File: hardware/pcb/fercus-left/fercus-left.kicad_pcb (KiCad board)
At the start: 2 copper layers, 133 x 133 mm, 274 parts, among them J1 USB_C_Receptacle_USB2.0, J2 USB_C_Receptacle_USB2.0, J3 Conn_01x06_MountingPin, J5 Conn_01x03, Q1 BSS138, Q10 BSS138, Q2 BSS138, Q3 BSS138, Q4 BSS138, Q5 BSS138, Q6 BSS138, Q7 BSS138, Q8 BSS138, Q9 BSS138, SW1 SW_Push, SW2 SW_Push, SW3 SW_Push, SW4 SW_Push, SW6 SW_Push, SW7 SW_SPDT, SW8 SW_Push, U1 XC6206P332MR, U2 CH32V208CBU6, U3 ETA9084E10, Y1 32MHz, Y2 32.768kHz

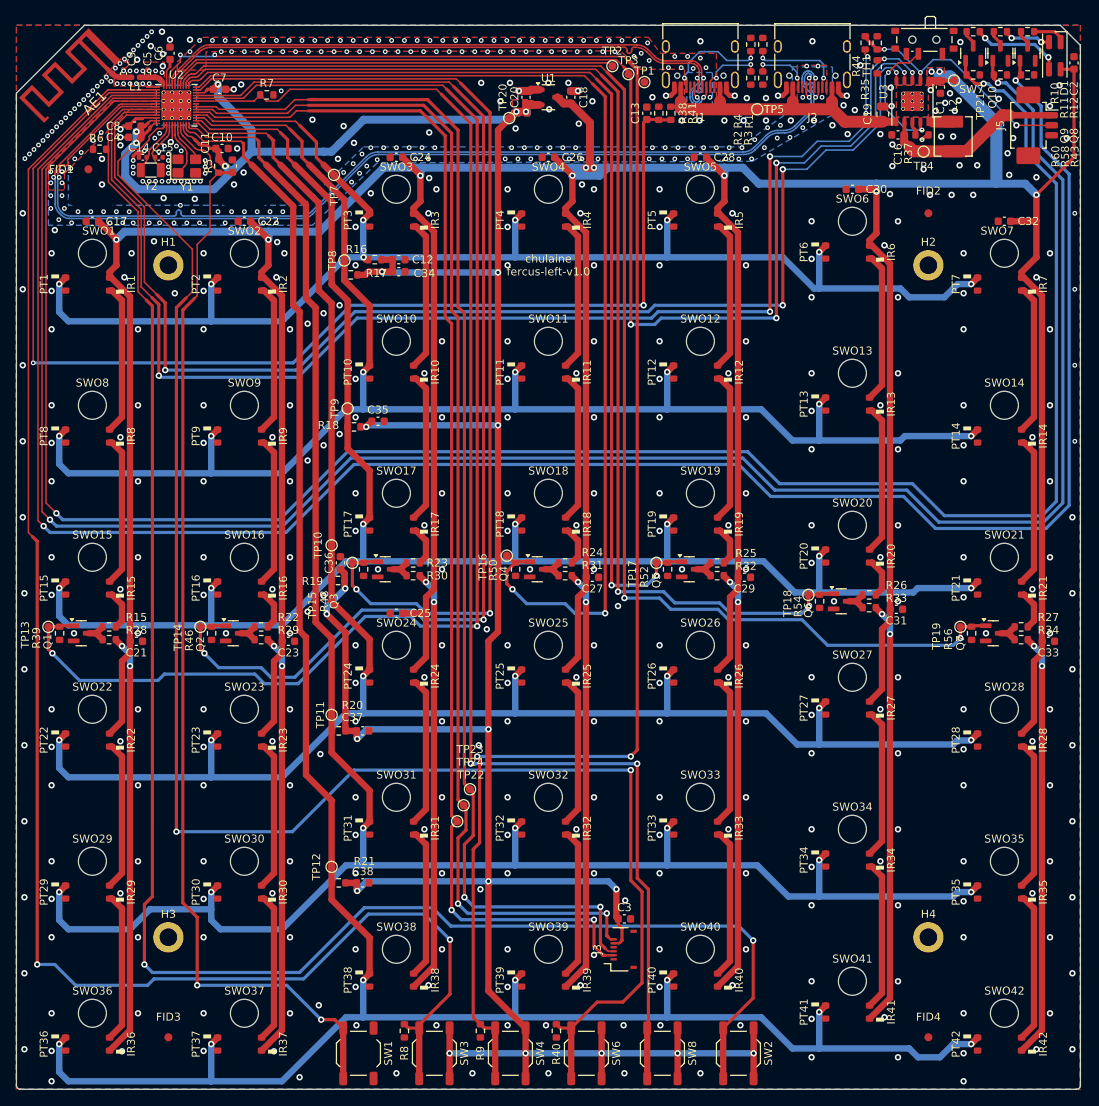
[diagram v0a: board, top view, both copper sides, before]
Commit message: merge
    fw:
    - fix usb product string, vid
    - add rf_phy_hop
    - add RF_BondingErase()
    - change default layout key fn to pause
    - fix power manager poweroff when usb disconnect
    - add usb compatibility interface

    hw:
    - change eta9084 iset resistor footprint to 0402
    - change fpc connector part
    - fix ir resistor value
    - change pcb thinkness to 1.6mm
    - fix footprint of pt and ir
    - fix rf ant trace
    - fix usb trace
    - add fercus-dongle-usb-c

    doc:
    - fix layout
    - add manual
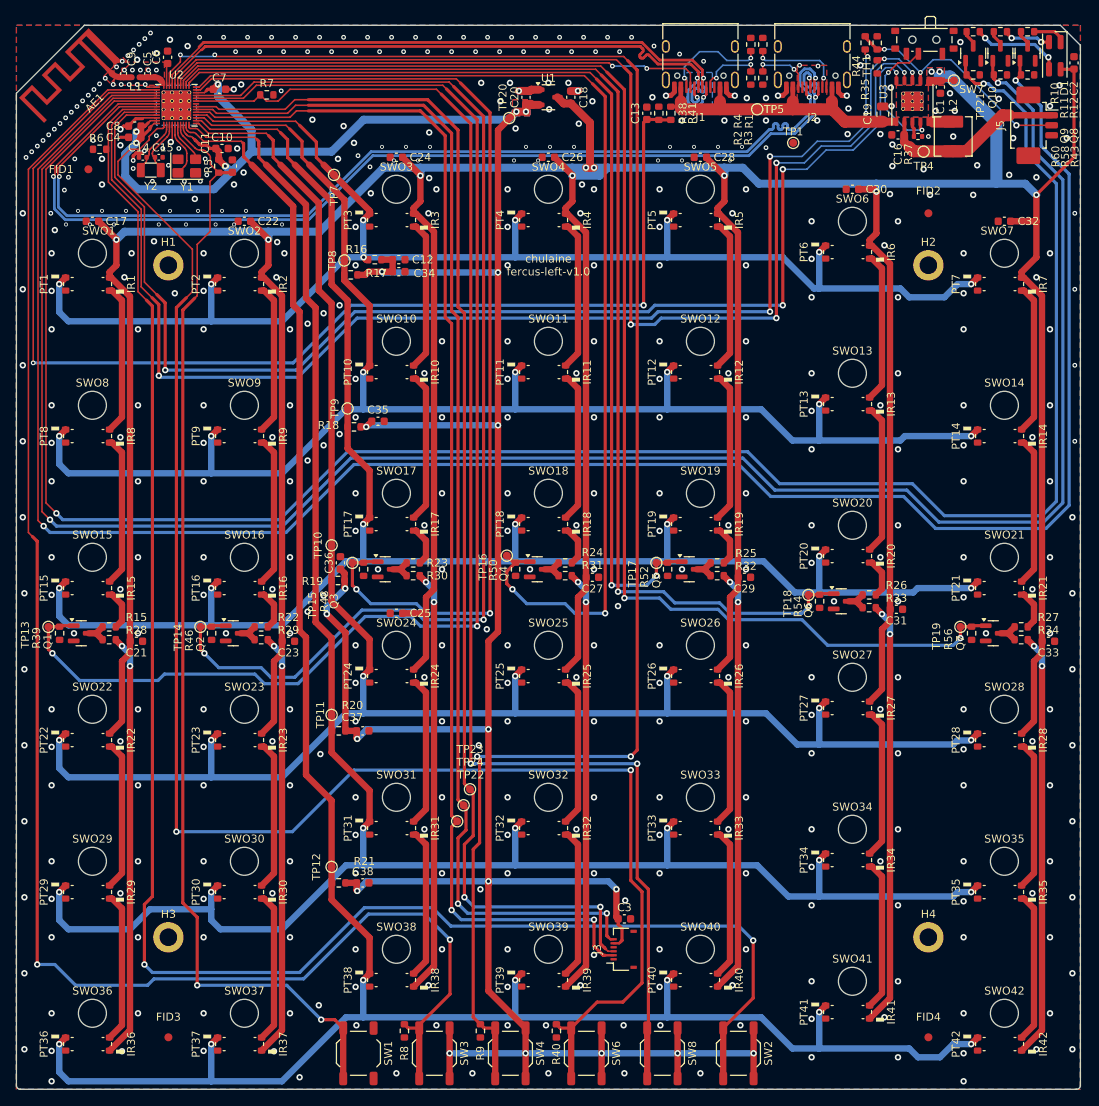
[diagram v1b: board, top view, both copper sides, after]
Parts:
- removed TP2, TP3: TestPoint, TestPoint:TestPoint_Pad_D1.0mm
- AE1: footprint chulaine:ANT-F-1-2.4G-1.2MM-FR4-WCH_Left_NoMask -> wch-ant:WCH_MIFA-1_2.4G_1.6mm_FR4_Left_NoMask
- IR1, IR10, IR11, IR12, IR13, IR14, IR15, IR16, IR17, IR18, IR19, IR2, IR20, IR21, IR22, IR23, IR24, IR25, IR26, IR27, IR28, IR29, IR3, IR30, IR31, IR32, IR33, IR34, IR35, IR36, IR37, IR38, IR39, IR4, IR40, IR41, IR42, IR5, IR6, IR7, IR8, IR9: value IR -> KTR-0602IRC-850
- J3: value Conn_01x06_MountingPin -> AFH34-S06FIA-1H
- J5: value Conn_01x03 -> Molex_PicoBlade_53261-0371_1x03-1MP_P1.25mm_Horizontal
- PT1, PT10, PT11, PT12, PT13, PT14, PT15, PT16, PT17, PT18, PT19, PT2, PT20, PT21, PT22, PT23, PT24, PT25, PT26, PT27, PT28, PT29, PT3, PT30, PT31, PT32, PT33, PT34, PT35, PT36, PT37, PT38, PT39, PT4, PT40, PT41, PT42, PT5, PT6, PT7, PT8, PT9: value Q_Photo_NPN_EC -> KTR-0602PTD
- R15, R22, R23, R24, R25, R26, R27, R28, R29, R30, R31, R32, R33, R34: value 69.8R -> 75R
- R37: value 2kR -> 2.49kR; footprint Resistor_SMD:R_0603_1608Metric -> Resistor_SMD:R_0402_1005Metric
- moved TP1 20.1 mm to (117.1, 34.7)
- moved C6 0.58 mm to (38.9, 24.0)
- moved R37 0.54 mm to (132.7, 33.9)
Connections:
- J1 pad A8: unconnected-(J1-SBU1-PadA8) -> usart1_tx
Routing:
- net usart1_tx: track 55.7 -> 67.7 mm, vias 0 -> 2
- net usb2_P: track 131.2 -> 133.6 mm
- net usb2_N: track 131.2 -> 133.6 mm
- net usb1_N: track 79.4 -> 80.9 mm
- net usb1_P: track 79.4 -> 80.9 mm
- net GND: track 27.1 -> 26.0 mm, vias 628 -> 495
- net /VINTA: track 3.43 -> 2.83 mm

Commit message: merge
hw:
- fix sch
- fix plate
- rename to fercus-dongle-usb-a

doc:
- add assembly
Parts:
- renumbered C12 to C21, C34 to C22, C35 to C23, C36 to C24, C37 to C25, C38 to C26, C21 to C31, C23 to C32, C25 to C33, C27 to C34, C29 to C35, C31 to C36, C33 to C37, C17 to C38, C22 to C39, C24 to C40, C26 to C41, C28 to C42, C30 to C43, C32 to C44, IR1 to D1, IR10 to D10, IR11 to D11, IR12 to D12, IR13 to D13, IR14 to D14, IR15 to D15, IR16 to D16, IR17 to D17, IR18 to D18, IR19 to D19, IR2 to D2, IR20 to D20, IR21 to D21, IR22 to D22, IR23 to D23, IR24 to D24, IR25 to D25, IR26 to D26, IR27 to D27, IR28 to D28, IR29 to D29, IR3 to D3, IR30 to D30, IR31 to D31, IR32 to D32, IR33 to D33, IR34 to D34, IR35 to D35, IR36 to D36, IR37 to D37, IR38 to D38, IR39 to D39, IR4 to D4, IR40 to D40, IR41 to D41, IR42 to D42, D1 to D43, IR5 to D5, IR6 to D6, IR7 to D7, IR8 to D8, IR9 to D9, PT1 to Q1, PT10 to Q10, PT11 to Q11, PT12 to Q12, PT13 to Q13, PT14 to Q14, PT15 to Q15, PT16 to Q16, PT17 to Q17, PT18 to Q18, PT19 to Q19, PT2 to Q2, PT20 to Q20, PT21 to Q21, PT22 to Q22, PT23 to Q23, PT24 to Q24, PT25 to Q25, PT26 to Q26, PT27 to Q27, PT28 to Q28, PT29 to Q29, PT3 to Q3, PT30 to Q30, PT31 to Q31, PT32 to Q32, PT33 to Q33, PT34 to Q34, PT35 to Q35, PT36 to Q36, PT37 to Q37, PT38 to Q38, PT39 to Q39, PT4 to Q4, PT40 to Q40, PT41 to Q41, PT42 to Q42, Q1 to Q43, Q2 to Q44, Q3 to Q45, Q4 to Q46, Q5 to Q47, Q6 to Q48, Q7 to Q49, PT5 to Q5, Q8 to Q50, Q9 to Q51, Q10 to Q52, PT6 to Q6, PT7 to Q7, PT8 to Q8, PT9 to Q9, SWO1 to SW1, SWO10 to SW10, SWO11 to SW11, SWO12 to SW12, SWO13 to SW13, SWO14 to SW14, SWO15 to SW15, SWO16 to SW16, SWO17 to SW17, SWO18 to SW18, SWO19 to SW19, SWO2 to SW2, SWO20 to SW20, SWO21 to SW21, SWO22 to SW22, SWO23 to SW23, SWO24 to SW24, SWO25 to SW25, SWO26 to SW26, SWO27 to SW27, SWO28 to SW28, SWO29 to SW29, SWO3 to SW3, SWO30 to SW30, SWO31 to SW31, SWO32 to SW32, SWO33 to SW33, SWO34 to SW34, SWO35 to SW35, SWO36 to SW36, SWO37 to SW37, SWO38 to SW38, SWO39 to SW39, SWO4 to SW4, SWO40 to SW40, SWO41 to SW41, SWO42 to SW42, SW1 to SW43, SW2 to SW44, SW8 to SW45, SW3 to SW46, SW4 to SW47, SW6 to SW48, SW7 to SW49, SWO5 to SW5, SWO6 to SW6, SWO7 to SW7, SWO8 to SW8, SWO9 to SW9
